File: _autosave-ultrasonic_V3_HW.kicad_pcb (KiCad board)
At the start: 2 copper layers, 206 parts, among them J1 Conn_02x20_Odd_Even, J2 Conn_Coaxial, J3 Conn_Coaxial, J4 Conn_01x07_Pin, J5 Screw_Terminal_01x02, J6 Conn_Coaxial, J7 Conn_Coaxial, Q10 NMOS, Q11 NMOS, Q12 NMOS, Q13 NMOS, Q14 NMOS, Q15 NMOS, Q16 NMOS, Q17 NMOS, Q18 NMOS, Q19 NMOS, Q2 NMOS, Q20 NMOS, Q21 NMOS, Q22 NMOS, Q3 NMOS, Q4 NMOS, Q5 NMOS, Q6 NMOS, Q7 NMOS, Q8 NMOS, Q9 NMOS, U1 MACHXO2-1200HC-4TG100C, U10 MIC4604YM, U11 MIC4604YM, U12 OKI-78SR-3.3_1.5-W36H-C, U13 OKI-78SR-12_1.0-W36H-C, U14 MCP1501-30xSN, U15 LM34966, U2 TDC_7200, U4 TLV3501AID, U5 DGS0010A, U6 OPA2392, U7 ADC10065, U8 MIC4604YM, U9 MIC4604YM, X1 16MHz

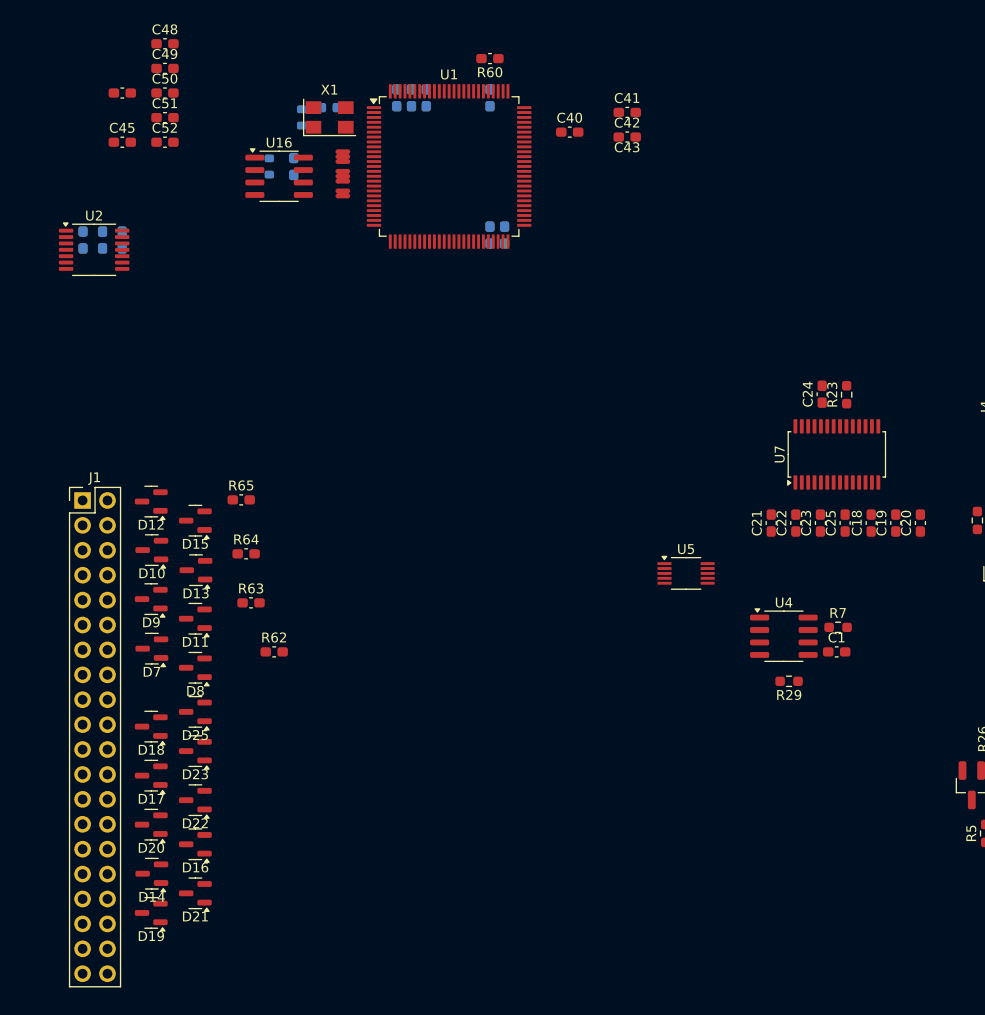
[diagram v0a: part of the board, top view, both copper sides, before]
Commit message: ready schematic for layout
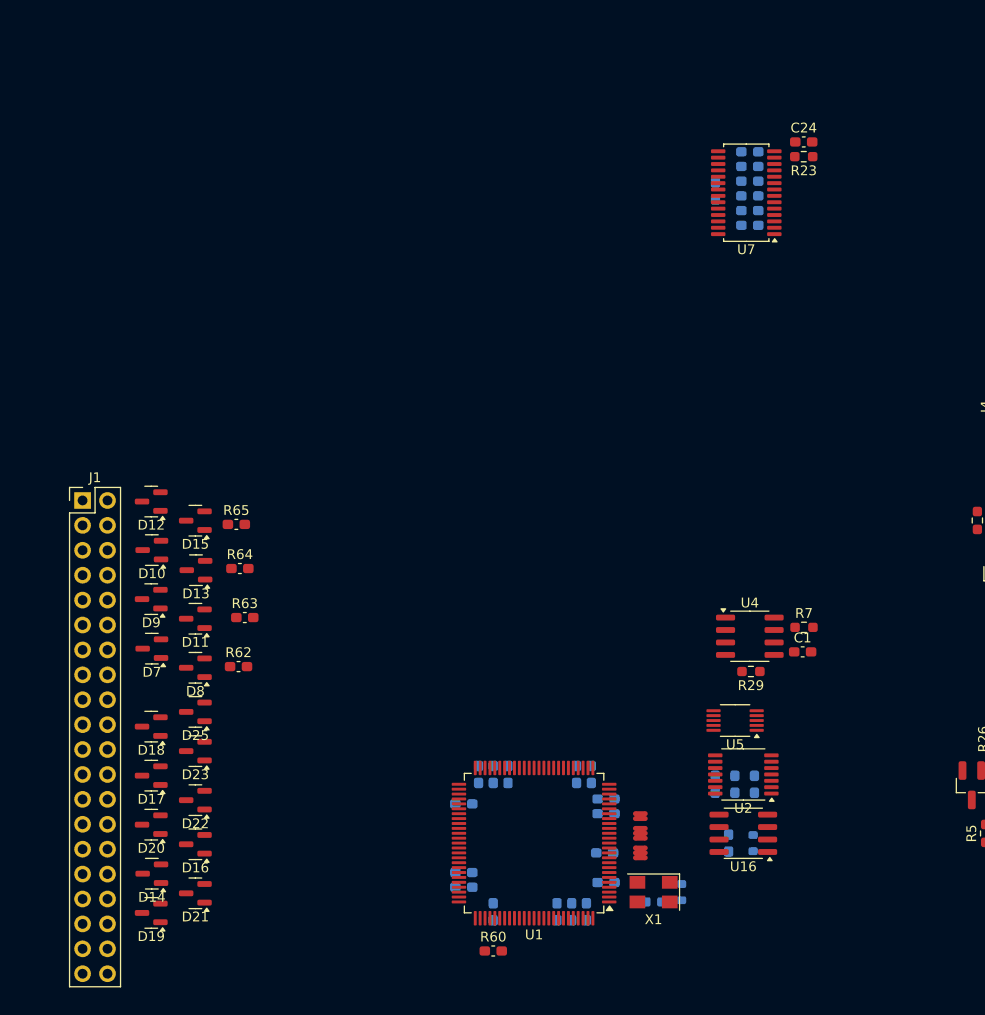
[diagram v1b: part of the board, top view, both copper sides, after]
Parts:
- C18, C19, C20, C21, C22, C23, C25, C40, C41, C42, C43, C45, C48, C49, C50, C51, C52: moved to B.Cu
- moved C50 92.2 mm to (160.3, 110.0)
- moved R60 91.0 mm to (148.8, 117.0), turned to 0 degrees
- moved C49 88.3 mm to (160.3, 103.0)
- moved C34 88.1 mm to (175.5, 100.0), turned to 90 degrees
- moved R61 88.0 mm to (168.0, 111.0), turned to 90 degrees
- moved C4 87.5 mm to (165.2, 112.0), turned to 0 degrees
- moved C51 87.4 mm to (160.2, 107.0)
- moved C48 86.3 mm to (158.8, 99.0), turned to 90 degrees
- moved X1 85.6 mm to (165.2, 111.0), turned to 180 degrees
- moved C39 85.2 mm to (158.3, 113.0), turned to -90 degrees
- moved U2 85.1 mm to (174.3, 99.0), turned to 180 degrees
- moved C35 85.1 mm to (173.5, 100.0), turned to 90 degrees
- moved R66 84.8 mm to (175.3, 106.0), turned to 90 degrees
- moved C37 84.6 mm to (156.8, 113.0), turned to -90 degrees
- moved C47 84.1 mm to (155.3, 113.0), turned to -90 degrees
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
